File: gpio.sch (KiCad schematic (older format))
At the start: 13 parts, among them J16 Rain, J17 GPIO, J18 Wind, U4 PCA9536D

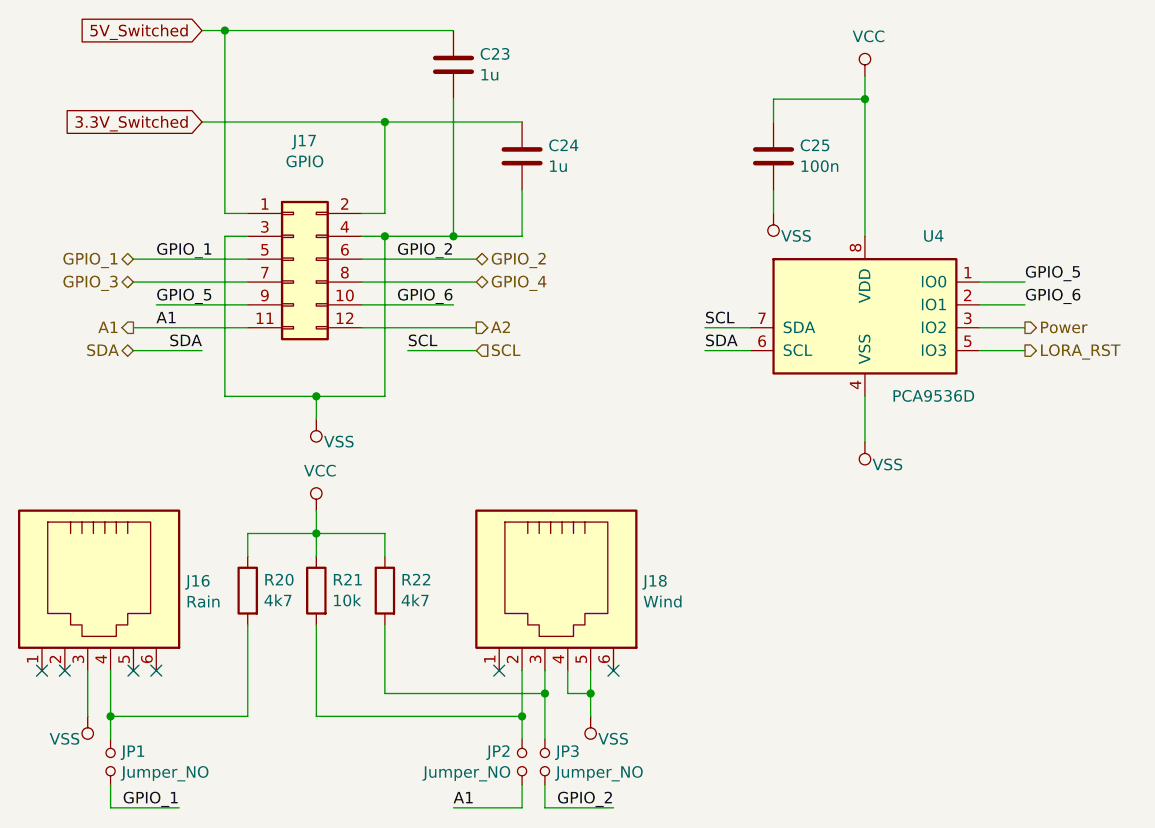
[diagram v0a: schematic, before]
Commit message: Swaped two wrong I2C signals.
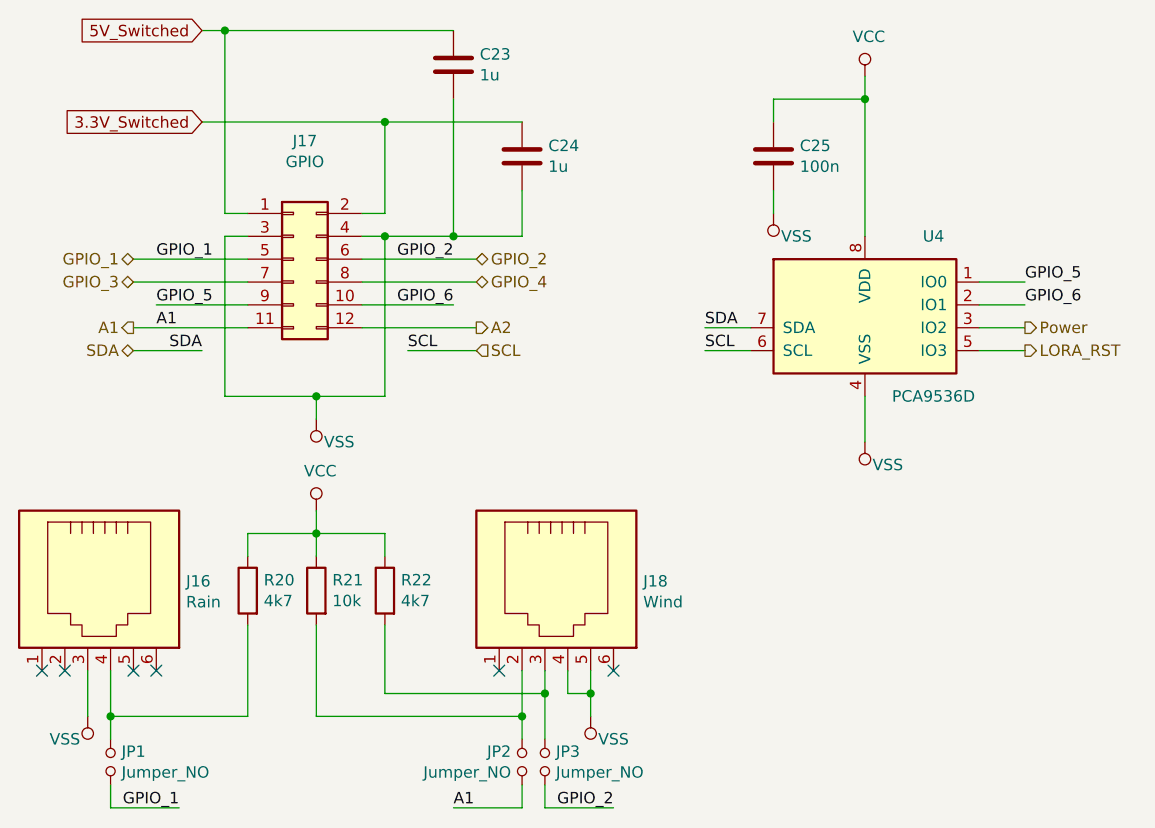
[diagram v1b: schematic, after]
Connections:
- net SCL: now also U4.6 (SCL); no longer U4.7 (SDA)
- net SDA: now also U4.7 (SDA); no longer U4.6 (SCL)
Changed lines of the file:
@@
 Sheet 9 12
 Title "AirMon"
-Date "2020-01-19"
-Rev "0.2"
+Date "2020-03-06"
+Rev "0.3"
 Comp "Jörg Bayer"
 Comment1 "CC BY 4.0"
@@
 SDA
 Wire Wire Line
-	6600 2600 6800 2600
+	6600 2700 6800 2700
+Text Label 6600 2700 0    50   ~ 0
+SCL
+Wire Wire Line
+	6800 2600 6600 2600
 Text Label 6600 2600 0    50   ~ 0
-SCL
-Wire Wire Line
-	6800 2700 6600 2700
-Text Label 6600 2700 0    50   ~ 0
 SDA
 Text HLabel 8000 2600 2    50   Output ~ 0
